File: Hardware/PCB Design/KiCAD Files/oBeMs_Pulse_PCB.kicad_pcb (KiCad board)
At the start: 2 copper layers, 180.3 x 120.7 mm, 134 parts, among them P1 1WIRE, P10 5V, P11 3V3, P12 GND, P13 ADC_0-7, P14 ADC_8-15, P15 ADC_VREF_2, P16 ADC_VREF_1, P17 SPI_ADC_DAC, P18 DIO_OUTPUT, P19 PULL_UP, P2 EXT_CAP, P20 GROUND, P21 DIO_INPUT, P22 DIO_OUTPUT, P23 PULL_UP, P24 GROUND, P25 DIO_INPUT, P26 DIO_OUTPUT, P27 PULL_UP, P28 GROUND, P29 DIO_INPUT, P3 HARD_WDT, P30 UNREG_DC, P31 V2?, P34 DAC, P36 PROTOTYPING_AREA, P4 LED 5-8, P6 AC_INPUT, P7 LED 1-4, P8 LT_PWR, P9 V1?, Q1 BC546, Q2 BC556, U1 LM2575, U2 DS18B20, U3 TLC555, U4 4017, U5 MCP3008, U6 MCP3008, U7 MCP4802, U8 LM2576

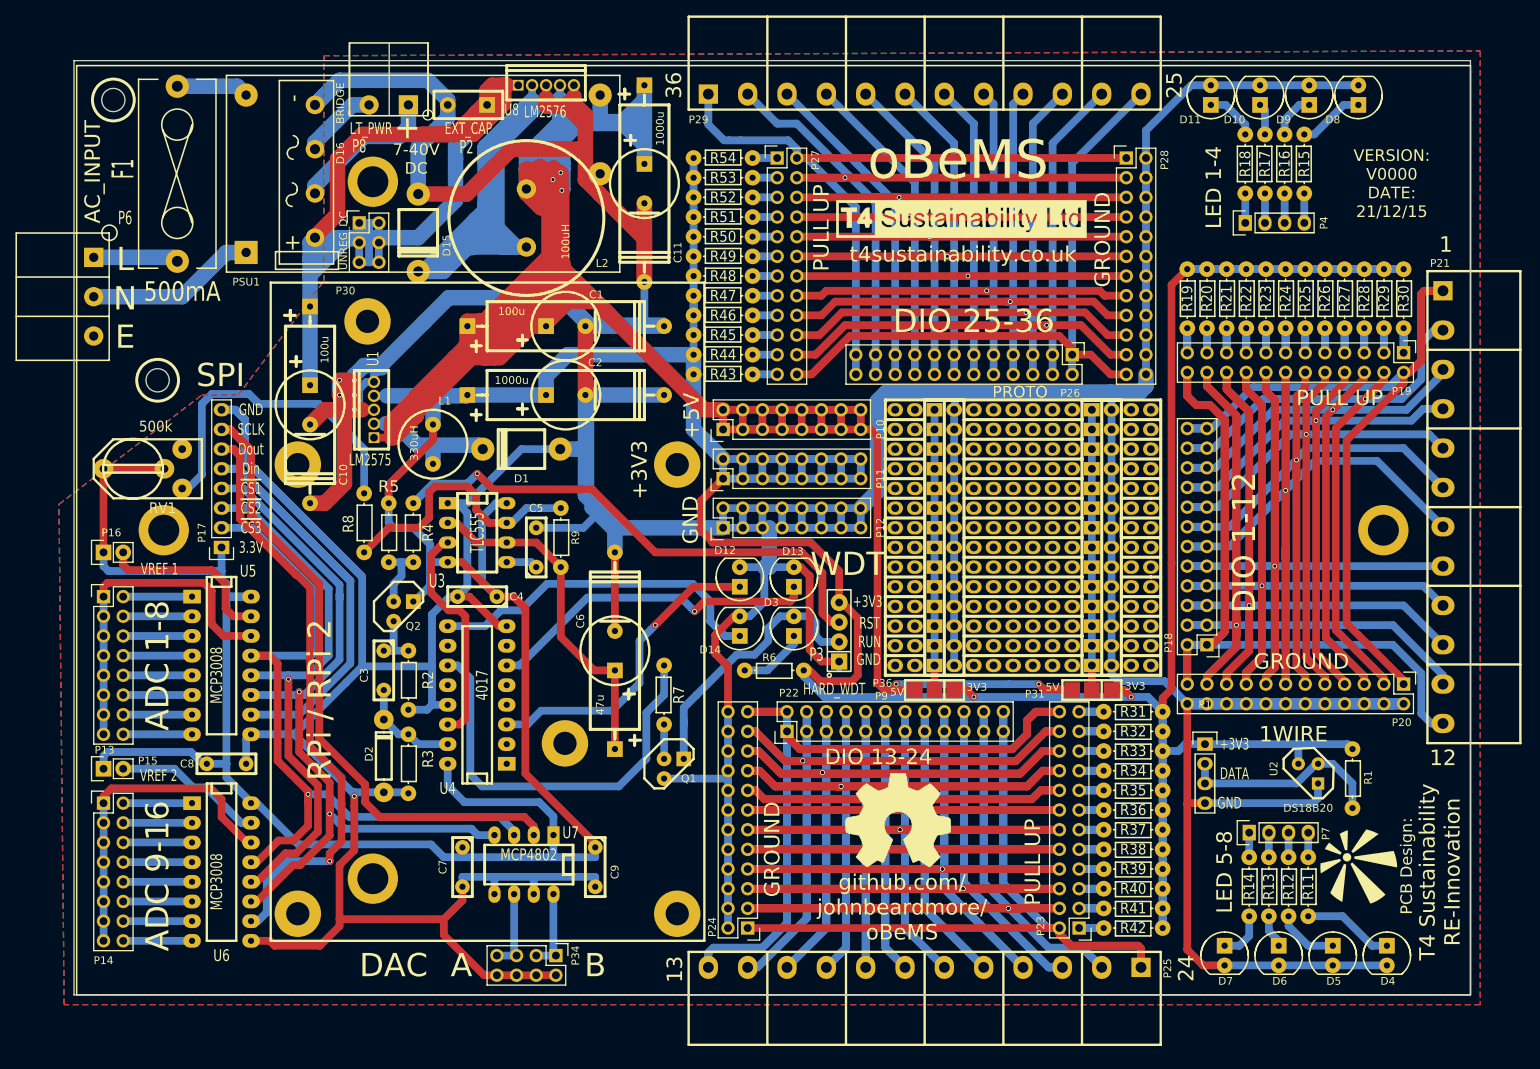
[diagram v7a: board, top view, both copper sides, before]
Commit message: Changes for v0001
Multiple PCb changes. 50Pcs ordered
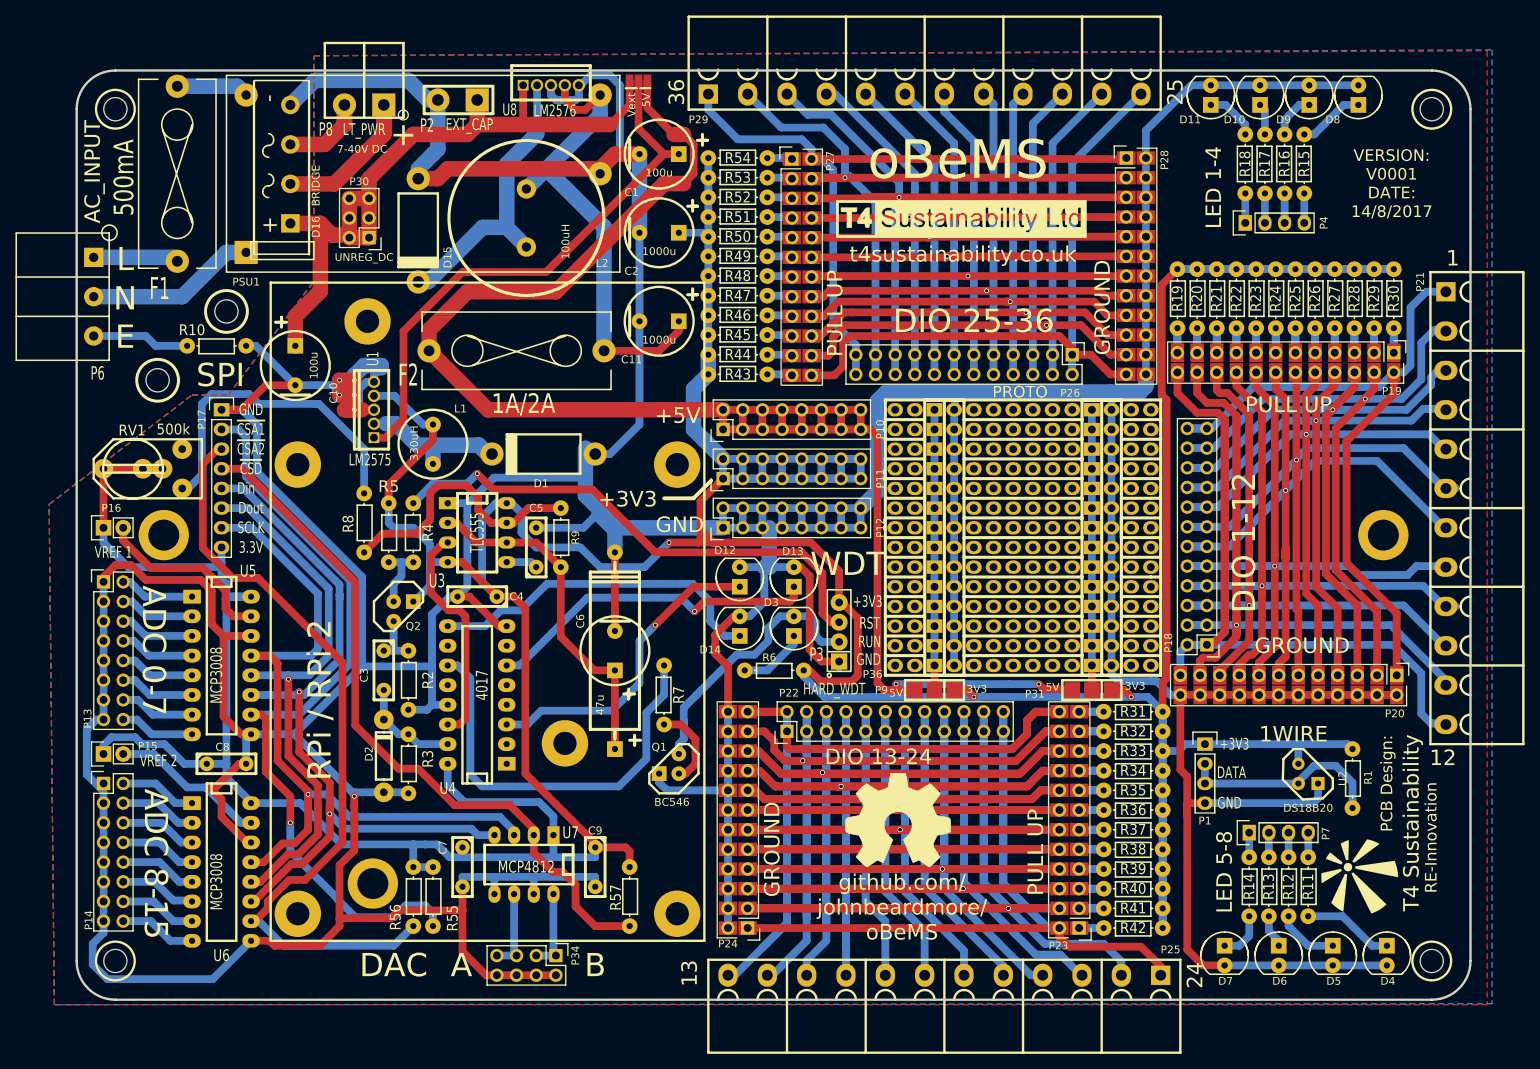
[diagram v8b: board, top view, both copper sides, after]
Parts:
- added F2: 1A/2A, REInnovationFootprint:TH_Fuse_Holder_5-20_CPC, F.Cu at (129.5, 73.0)
- added P32: V_PWR, REInnovationFootprint:SM_3pad_SOLDER_named, F.Cu at (146.7, 38.1)
- added R10: 1M, REInnovationFootprint:TH_Resistor_1, F.Cu at (90.8, 72.4)
- added R55: 100k, REInnovationFootprint:TH_Resistor_1, F.Cu at (118.7, 143.5)
- added R56: 100k, REInnovationFootprint:TH_Resistor_1, F.Cu at (116.2, 143.5)
- added R57: 100k, REInnovationFootprint:TH_Resistor_1, F.Cu at (144.1, 143.5)
- C1, C10, C11: footprint REInnovationFootprint:C2V8_VandA -> REInnovationFootprint:C2V8_V
- C2: footprint REInnovationFootprint:C2V8_VandA -> C2V8_V
- C4: value 0.1u -> 1u
- C5: value 10n -> 1u
- C7, C8: value 1000n -> 1u
- C9: value 100n -> 1u
- D16: footprint REInnovationFootprint:TH_BridgeRect_8A -> TH_BridgeRect_8A
- P19, P20, P23, P24, P27, P28: footprint REInnovationFootprint:Pin_Header_Straight_2x12 -> REInnovationFootprint:Pin_Header_Straight_2x12_SM_Connect
- P2: footprint matts_components:SIL-2_wide_lg_pad -> REInnovationFootprint:SIL-2_LG_PAD
- P8: footprint REInnovationFootprint:TH_CONN_2W -> REInnovationFootprint:TH_CONN_2W_LGPAD
- Q1: footprint matts_components:TO92-EBC_large_pad -> matts_components:TO92-PNP_large_pad
- RV1: footprint matts_components:RV_various_lg_pad -> REInnovationFootprint:RV_various_lg_pad
- U7: value MCP4802 -> MCP4812
- moved H2 31.0 mm to (92.1, 67.9)
- moved C1 25.3 mm to (148.0, 47.6), turned to 180 degrees
- moved C2 24.2 mm to (148.0, 57.8), turned to 180 degrees
- moved C11 17.9 mm to (148.0, 69.2), turned to 180 degrees
- moved P17 17.8 mm to (91.4, 80.6), turned to 0 degrees
- moved C10 5.43 mm to (101.0, 74.9)
- moved D16 3.17 mm to (100.3, 41.3)
- moved P16 3.17 mm to (76.2, 95.9)
- moved P8 3.17 mm to (107.3, 41.3)
- moved P25 2.74 mm to (212.7, 153.7)
- moved D1 2.62 mm to (132.7, 86.4)
- moved P14 2.54 mm to (76.2, 128.9)
- moved P30 2.29 mm to (110.5, 58.4), turned to 180 degrees
- moved P27 1.91 mm to (165.1, 48.3)
- moved P13 1.91 mm to (76.2, 102.9)
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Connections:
- C1 pad 1: +5V -> Net-(C1-Pad1)
- C11 pad 1: +5V -> Net-(C11-Pad1)
- L2 pad 2: +5V -> Net-(C11-Pad1)
- P13 pad 1: Net-(P13-Pad1) -> GND
- P13 pad 11: Net-(P13-Pad1) -> GND
- P13 pad 13: Net-(P13-Pad1) -> GND
- P13 pad 15: Net-(P13-Pad1) -> GND
- P13 pad 3: Net-(P13-Pad1) -> GND
- P13 pad 5: Net-(P13-Pad1) -> GND
- P13 pad 7: Net-(P13-Pad1) -> GND
- P13 pad 9: Net-(P13-Pad1) -> GND
- P14 pad 1: Net-(P14-Pad1) -> GND
- P14 pad 11: Net-(P14-Pad1) -> GND
- P14 pad 13: Net-(P14-Pad1) -> GND
- P14 pad 15: Net-(P14-Pad1) -> GND
- P14 pad 3: Net-(P14-Pad1) -> GND
- P14 pad 5: Net-(P14-Pad1) -> GND
- P14 pad 7: Net-(P14-Pad1) -> GND
- P14 pad 9: Net-(P14-Pad1) -> GND
- P17 pad 1: +3.3V -> GND
- P17 pad 8: GND -> +3.3V
- PCB1 pad 1: Net-(PCB1-Pad1) -> (no net)
- PSU1 pad 3: +5V -> Net-(C11-Pad1)
- Q1 pad 1: GND -> /Watch Dog Timer/WDT_OUT
- Q1 pad 3: /Watch Dog Timer/WDT_OUT -> GND
- RV1 pad 3: Net-(RV1-Pad3) -> (no net)
- U1 pad 1: +5V -> Net-(C1-Pad1)
- U2 pad 1: +3.3V -> GND
- U2 pad 3: GND -> +3.3V
- U4 pad 1: Net-(U4-Pad1) -> (no net)
- U4 pad 10: Net-(U4-Pad10) -> (no net)
- U4 pad 12: Net-(U4-Pad12) -> (no net)
- U4 pad 2: Net-(U4-Pad2) -> (no net)
- U4 pad 4: Net-(U4-Pad4) -> (no net)
- U4 pad 5: Net-(U4-Pad5) -> (no net)
- U4 pad 7: Net-(U4-Pad7) -> (no net)
- U5 pad 10: Net-(P17-Pad5) -> Net-(P17-Pad2)
- U5 pad 11: Net-(P17-Pad4) -> Net-(P17-Pad5)
- U5 pad 12: Net-(P17-Pad3) -> Net-(P17-Pad6)
- U5 pad 13: Net-(P17-Pad2) -> Net-(P17-Pad7)
- U5 pad 14: Net-(P13-Pad1) -> GND
- U6 pad 10: Net-(P17-Pad6) -> Net-(P17-Pad3)
- U6 pad 11: Net-(P17-Pad4) -> Net-(P17-Pad5)
- U6 pad 12: Net-(P17-Pad3) -> Net-(P17-Pad6)
- U6 pad 13: Net-(P17-Pad2) -> Net-(P17-Pad7)
- U6 pad 14: Net-(P14-Pad1) -> GND
- U7 pad 2: Net-(P17-Pad7) -> Net-(P17-Pad4)
- U7 pad 3: Net-(P17-Pad2) -> Net-(P17-Pad7)
- U7 pad 4: Net-(P17-Pad4) -> Net-(P17-Pad5)
- U8 pad 4: +5V -> Net-(C11-Pad1)
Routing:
- net +5V: track 530.8 -> 234.2 mm, vias 5 -> 2
- net Net-(C10-Pad1): track 196.0 -> 105.3 mm
- net Net-(C1-Pad1): track 0.00 -> 72.1 mm
- net Net-(C11-Pad1): track 0.00 -> 62.3 mm
- net Net-(D15-Pad2): track 96.8 -> 37.9 mm
- net Net-(P13-Pad1): track 45.0 -> 0.00 mm
- net Net-(P14-Pad1): track 42.4 -> 0.00 mm
- net Net-(P18-Pad10): track 120.6 -> 80.1 mm
- net Net-(P18-Pad11): track 128.7 -> 89.1 mm
- net Net-(P17-Pad6): track 109.8 -> 73.0 mm
- net GND: track 1117.1 -> 1081.3 mm
- net Net-(P17-Pad3): track 73.1 -> 101.3 mm, vias 1 -> 0
- net Net-(P22-Pad10): track 151.5 -> 131.9 mm
- net Net-(P22-Pad11): track 151.8 -> 132.6 mm
- net Net-(P22-Pad13): track 155.6 -> 137.8 mm
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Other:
- board size 180.3 x 120.7 mm -> 180 x 120 mm
- net class Default: clearance 0.2 -> 0.1
- rule trace_clearance: 0.2 -> 0.1
- board text added: "ADC 0-7"
- board text added: "ADC 8-15"
- board text added: "RE-Innovation"
- board text added: "T4 Sustainability"
- board text added: "VERSION: V0001 DATE: 14/8/2017"
- board text added: "~CSA1"
- board text added: "~CSA2"
- board text added: "~CSD"
- board text removed: "ADC 1-8"
- board text removed: "ADC 9-16"
- board text removed: "T4 Sustainability RE-Innovation"
- board text removed: "VERSION: V0000 DATE: 21/12/15"
- board text removed: "~CS1"
- board text removed: "~CS2"
- board text removed: "~CS3"
